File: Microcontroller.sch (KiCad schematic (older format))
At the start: 38 parts, among them J2 USB_OTG, J3 Conn_01x05, J4 JST_XH-04, J5 JST_XH-04, Q3 PMV50XPR, Q4 PMV50XPR, SW1 SW_Push, SW2 SW_Push, U1 AP2210N-3.3, U2 STM32F070CBT6, Y1 8MHz

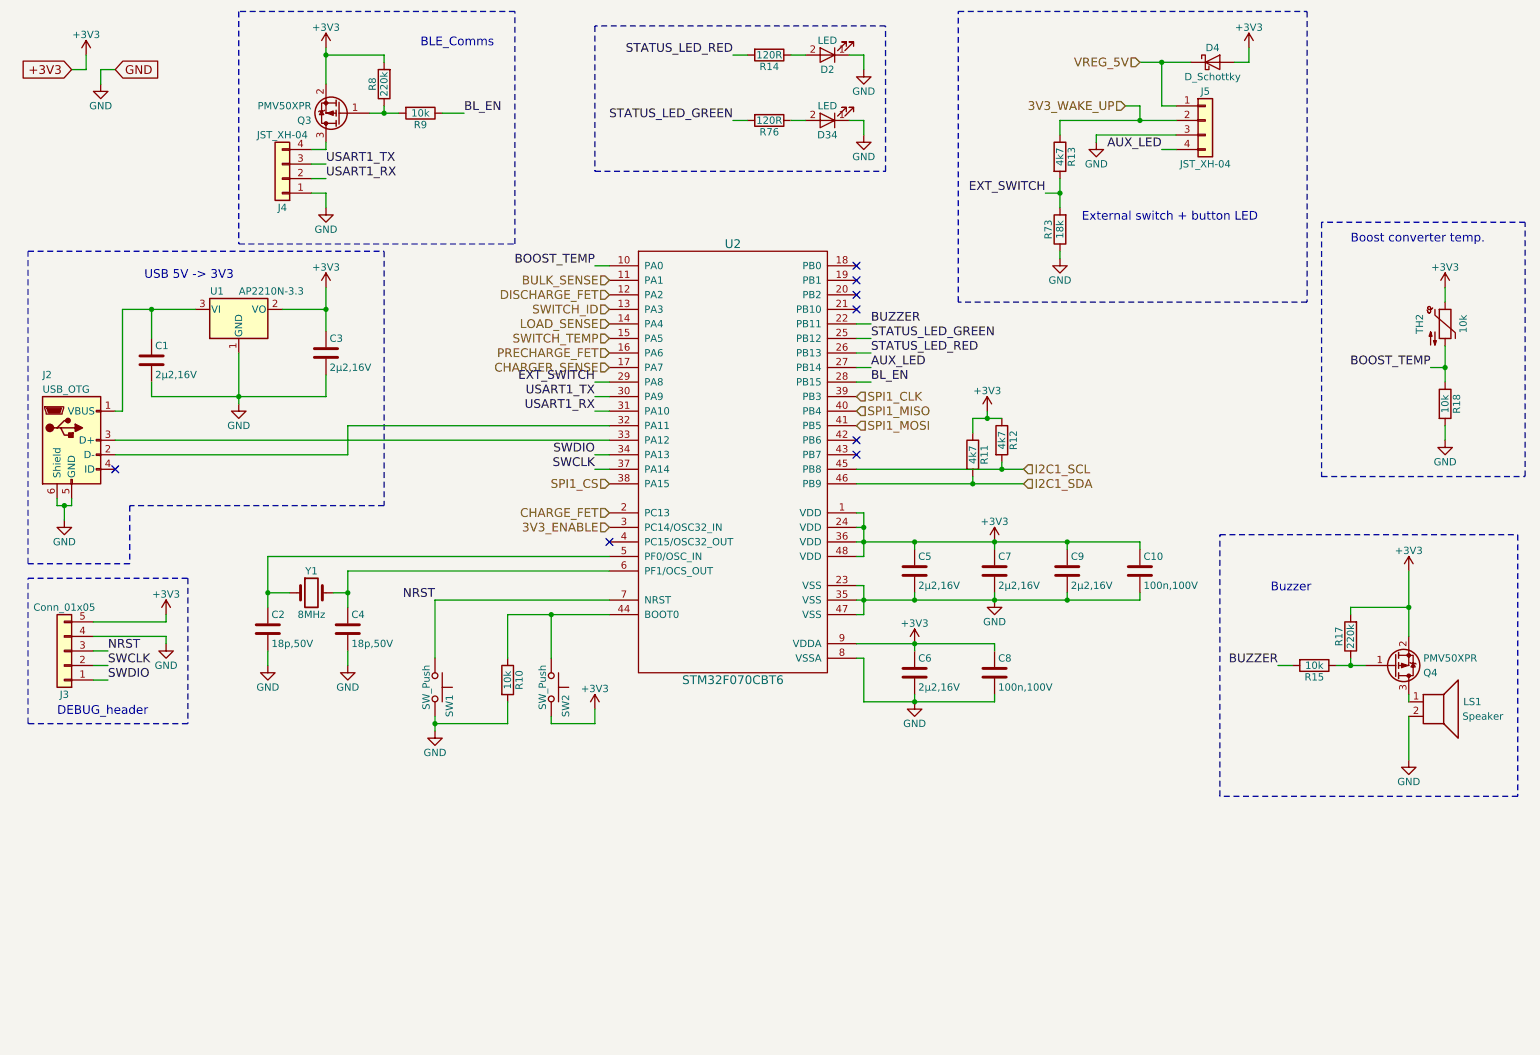
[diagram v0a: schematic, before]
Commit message: HW 0.2 finalized schematic and pcb files, BOM needs to be checked
Lots of major and little problems fixed found in the 0.1

Major changes:
-LTC6803-3 footprint changed to it's correct one
-Boost converter layout and capacitor optimization
-MCU switched from STM32F070CBT6 to ultra low power STM32L433CCT6 to improve sleep state power consumption
-Button/LED + Comms connectors switched from THT JST-XH to SMD JST-PH
-CAN-bus support added
-Changed power regulator setup for "always on"

Minor changes:
-Changed cell balance resistor sizes from 0603 to 0402 in order to get a bit more breathing room during soldering
-External oscillator removed from MCU, because new one has everything available internally
-Comms connector has USART or CAN available via solder bridges
-Sense resistors switched to higher resistance ones to lower deep sleep standby current
-etc.
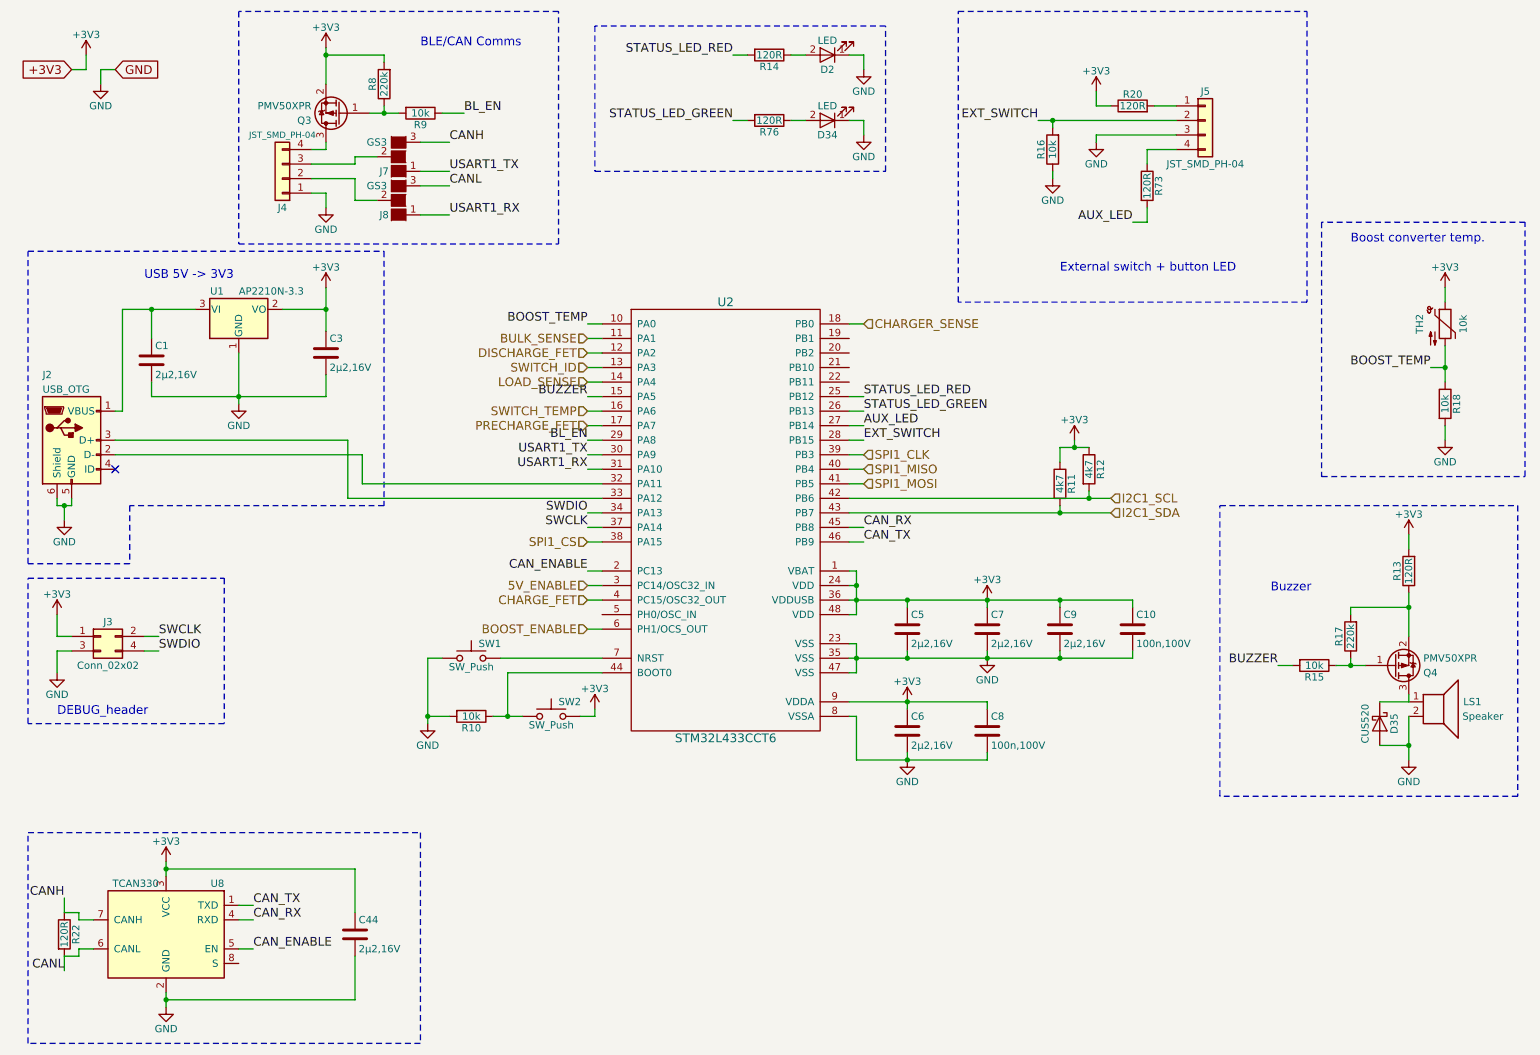
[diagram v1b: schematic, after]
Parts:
- removed C2, C4: 18p,50V, Capacitors_SMD:C_0603, symbol C
- removed D4: D_Schottky, Diodes_SMD:D_SOD-323, symbol D_Schottky
- removed J3: Conn_01x05, Pin_Headers:Pin_Header_Straight_1x05_Pitch2.54mm_SMD_Pin1Left, symbol Conn_01x05
- removed U2: STM32F070CBT6, Housings_QFP:LQFP-48_7x7mm_Pitch0.5mm, symbol STM32F070CBT6
- removed Y1: 8MHz, Crystals:Crystal_SMD_5032-2pin_5.0x3.2mm, symbol Crystal
- added C44: 2µ2,16V, Capacitors_SMD:C_0603, symbol C
- added D35: CUS520, Diodes_SMD:D_SOD-323, symbol D_Schottky
- added J3: Conn_02x02, Socket_Strips:Socket_Strip_Straight_2x02_Pitch2.54mm_SMD, symbol Conn_02x02_Odd_Even
- added J7, J8: GS3, Connectors:GS3, symbol GS3
- added R16: 10k, Resistors_SMD:R_0603, symbol R
- added R20, R22: 120R, Resistors_SMD:R_0603, symbol R
- added U2: STM32L433CCT6, Housings_QFP:LQFP-48_7x7mm_Pitch0.5mm, symbol STM32L433CCT6
- added U8: TCAN330, TO_SOT_Packages_SMD:SOT-23-8, symbol TJA1051T/E
- C1, C3, C5, C6, C7, C9: MFG EMK107BJ225KA-T -> ANY; TempCo. (none) -> X5R
- C10, C8: MFG CL10B104KC8NNNC -> ANY; TempCo. (none) -> X7R
- J4, J5: value JST_XH-04 -> JST_SMD_PH-04; footprint Connectors_JST:JST_XH_B04B-XH-A_04x2.50mm_Straight -> Connectors_JST:JST_PH_B4B-PH-SM4-TB_04x2.00mm_Straight
- R10, R15, R18, R9: MFG RC0603FR-0710KL -> ANY; Tol. (none) -> 1%
- R11, R12: MFG RC0603FR-074K7L -> ANY; Tol. (none) -> 1%
- R13: value 4k7 -> 120R; MFG RC0603FR-074K7L -> ANY; Tol. (none) -> 1%
- R14, R76: MFG RC0603FR-07120RL -> ANY; Tol. (none) -> 1%
- R17, R8: MFG RC0603FR-07220KL -> ANY; Tol. (none) -> 1%
- R73: value 18k -> 120R; MFG RC0603FR-0718KL -> ANY; Tol. (none) -> 1%
- TH2: B25/85 (none) -> 4300K; Tol. (none) -> 5%
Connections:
- net NRST is gone; now on net GND: SW1.1
- net +3V3: now also R13.2, C44.1, J3.1 (Pin_1), R20.1, U2.1 (VBAT), U2.24 (VDD), U2.36 (VDDUSB), U2.48 (VDD), U2.9 (VDDA), U8.3 (VCC); no longer Q4.2 (S), R17.2
- net AUX_LED: now also R73.2, U2.27 (PB14); no longer J5.4 (Pin_4)
- net BL_EN: now also U2.29 (PA8)
- net BOOST_TEMP: now also U2.10 (PA0)
- net BULK_SENSE: now also U2.11 (PA1)
- net BUZZER: now also U2.15 (PA5)
- net CHARGER_SENSE: now also U2.18 (PB0)
- net CHARGE_FET: now also U2.4 (PC15/OSC32_OUT)
- net DISCHARGE_FET: now also U2.12 (PA2)
- net EXT_SWITCH: now also J5.2 (Pin_2), R16.2, U2.28 (PB15); no longer R13.2, R73.2
- net GND: now also C44.2, D35.2 (A), J3.3 (Pin_3), R16.1, U2.23 (VSS), U2.35 (VSS), U2.47 (VSS), U2.8 (VSSA), U8.2 (GND); no longer R73.1, SW1.2
- net I2C1_SCL: now also U2.42 (PB6)
- net I2C1_SDA: now also U2.43 (PB7)
- net LOAD_SENSE: now also U2.14 (PA4)
- net PRECHARGE_FET: now also U2.17 (PA7)
- net SPI1_CLK: now also U2.39 (PB3)
- net SPI1_CS: now also U2.38 (PA15)
- net SPI1_MISO: now also U2.40 (PB4)
- net SPI1_MOSI: now also U2.41 (PB5)
- net STATUS_LED_GREEN: now also U2.26 (PB13)
- net STATUS_LED_RED: now also U2.25 (PB12)
- net SWCLK: now also J3.2 (Pin_2), U2.37 (PA14)
- net SWDIO: now also J3.4 (Pin_4), U2.34 (PA13)
- net SWITCH_ID: now also U2.13 (PA3)
- net SWITCH_TEMP: now also U2.16 (PA6)
- net USART1_RX: now also J8.1 (G1), U2.31 (PA10); no longer J4.2 (Pin_2)
- net USART1_TX: now also J7.1 (G1), U2.30 (PA9); no longer J4.3 (Pin_3)
- net at J2.2 (D-): now also U2.32 (PA11)
- net at J2.3 (D+): now also U2.33 (PA12)
- net at R10.1, SW2.1: now also U2.44 (BOOT0)
- net at LS1.1, Q4.3 (D): now also D35.1 (K)
- net 3V3_WAKE_UP: no longer names the net of R13.1
- net 3V3_WAKE_UP: now also Q4.2 (S), R17.2; no longer J5.2 (Pin_2)
- net VREG_5V: no longer names the net of J5.1 (Pin_1)
- net VREG_5V: now also R20.2
- new net: J5.4 (Pin_4), R73.1
- new net: SW1.2, U2.7 (NRST)
- new net: J4.2 (Pin_2), J8.2 (G2)
- new net: J4.3 (Pin_3), J7.2 (G2)
- new net 5V_ENABLE: U2.3 (PC14/OSC32_IN)
- new net BOOST_ENABLE: U2.6 (PH1/OCS_OUT)
- new net CANH: J7.3 (G3), R22.1, U8.7 (CANH)
- new net CANL: J8.3 (G3), R22.2, U8.6 (CANL)
- new net CAN_ENABLE: U2.2 (PC13), U8.5 (EN)
- new net CAN_RX: U2.45 (PB8), U8.4 (RXD)
- new net CAN_TX: U2.46 (PB9), U8.1 (TXD)
- no-connect marks 8 -> 1
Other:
- note added: "BLE/CAN Comms"
- note removed: "BLE_Comms"
- moved on the sheet: C10, C5, C6, C7, C8, C9, R10, R11, R12, SW1, SW2
